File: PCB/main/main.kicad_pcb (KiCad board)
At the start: 2 copper layers, 97 x 73 mm, 64 parts, among them IC1 LM358DT, IC2 LM358DT, IC3 AT24C256C-SSHL-T, IC4 FT230XS-R, IC5 MCP73831T-2ACI_OT, IC6 MCP1700T-3302E_TT, J1 Conn_01x33_Female, J10 PZ254V-11-02P, J2 Conn_01x33_Female, J3 Conn_01x33_Female, J4 Conn_01x33_Female, J5 47346-0001, J6 PZ254V-11-02P, J7 PZ254V-11-02P, J8 MTP125-1103S1, J9 PZ254V-11-02P, Q1 IRF9540NPbF

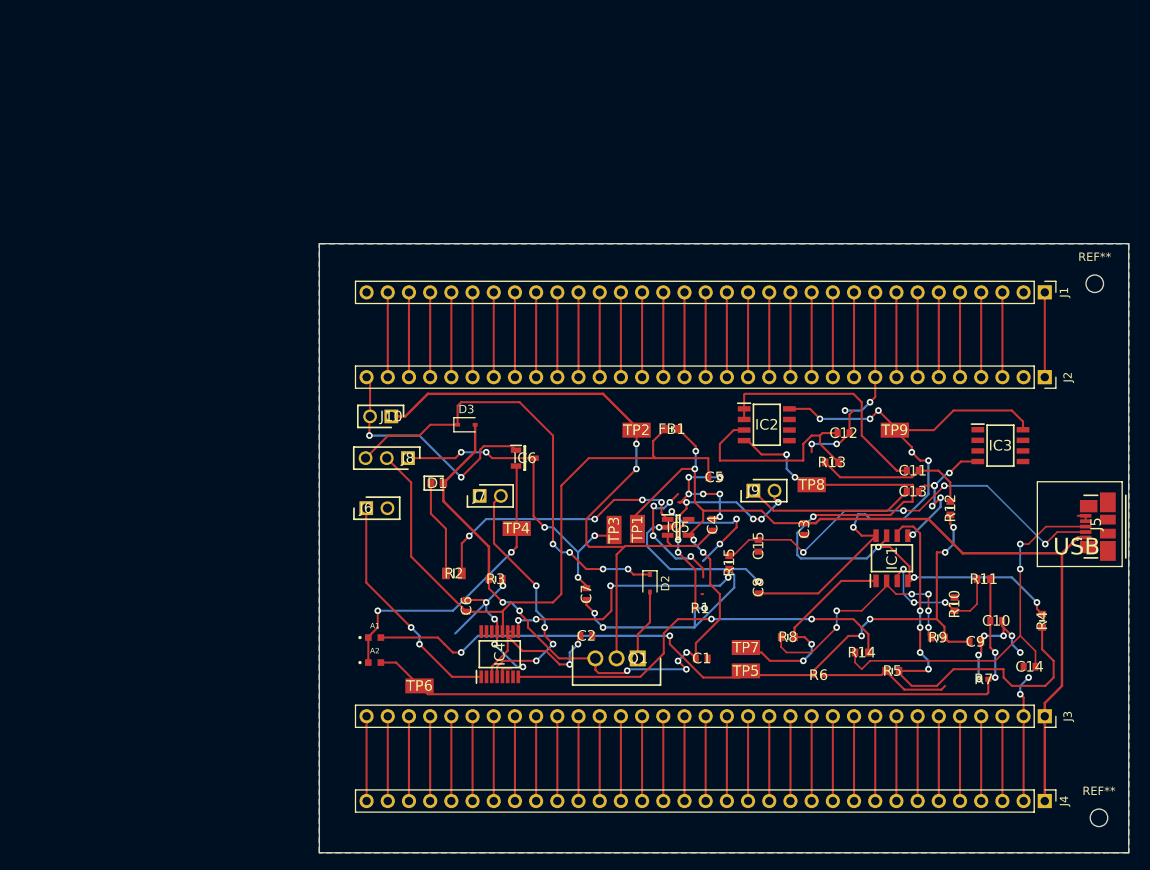
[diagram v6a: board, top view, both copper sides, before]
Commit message: changed power schematic
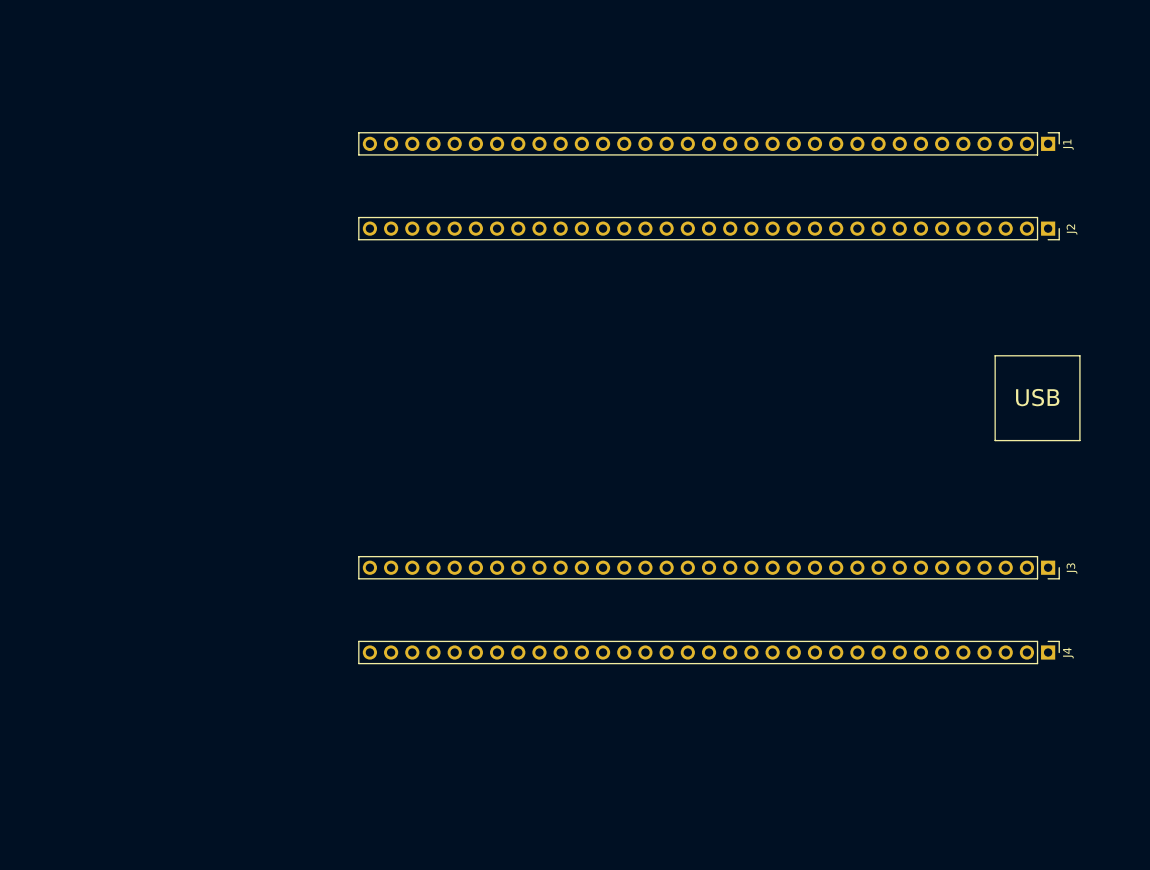
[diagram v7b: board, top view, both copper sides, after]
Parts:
- removed A1, A2: ALS-PT19-315C/L177/TR8, SamacSys_Parts:XDCR_ALS-PT19-315C_L177_TR8
- removed C1: 10nF, SamacSys_Parts:CAPC1608X90N
- removed C10, C9: CL10A105KB8NNNC, SamacSys_Parts:CAPC1608X90N
- removed C11, C12: CL10A335KP8NNNC, SamacSys_Parts:CAPC1608X90N
- removed C13, C2: CC0603KRX7R9BB104, SamacSys_Parts:CAPC1608X90N
- removed C14, C15: CL10C470JB8NNNC, SamacSys_Parts:CAPC1608X90N
- removed C3, C4, C6: CL10A475KA8NQNC, SamacSys_Parts_Microcontroller:CAPC1608X95N
- removed C5: 100nF, SamacSys_Parts:CAPC1608X90N
- removed C7, C8: 1uF, SamacSys_Parts:CAPC1608X90N
- removed D1: LED, SamacSys_Parts:LEDC1608X70N
- removed D2, D3: BAT60J, Diode_SMD:D_SOD-323
- removed FB1: Ferrite_Bead, SamacSys_Parts:BEADC1608X95N
- removed IC1, IC2: LM358DT, SamacSys_Parts:SOIC127P600X175-8N
- removed IC3: AT24C256C-SSHL-T, SamacSys_Parts:SOIC127P600X175-8N
- removed IC4: FT230XS-R, SamacSys_Parts_Power:SOP64P599X175-16N
- removed IC5: MCP73831T-2ACI_OT, SamacSys_Parts_Power:SOT95P270X145-5N
- removed IC6: MCP1700T-3302E_TT, SamacSys_Parts_Power:SOT95P237X112-3N
- removed J10, J6, J7, J9: PZ254V-11-02P, SamacSys_Parts_Power:HDRV2W64P0X254_1X2_508X250X873P
- removed J5: 47346-0001, SamacSys_Parts_Microcontroller:47346-0001
- removed J8: MTP125-1103S1, SamacSys_Parts_Power:HDRV3W64P0X254_1X3_762X250X885P
- removed Q1: IRF9540NPbF, SamacSys_Parts_Power:TO254P469X1042X1967-3P
- removed R1: 2k, SamacSys_Parts:RESC1005X35N
- removed R10, R11, R12, R13, R4, R5, R8, R9: RC0603FR-071KL, SamacSys_Parts:RESC1608X55N
- removed R14, R15: 0603WAF270JT5E, SamacSys_Parts:RESC1608X55N
- removed R2: RC0805FR-07470RL, SamacSys_Parts_Microcontroller:RESC2012X60N
- removed R3: 10k, SamacSys_Parts:RESC1608X55N
- removed R6, R7: AC0402FR-07536KL, SamacSys_Parts:RESC1005X37N
- removed REF** (x2): MountingHole_2.1mm, MountingHole:MountingHole_2.1mm
- removed TP1, TP2, TP3, TP4, TP5, TP6, TP7, TP8, TP9: 5017, SamacSys_Parts_Power:5017
- moved J4 17.8 mm to (180.3, 127.0)
- moved J1 17.8 mm to (180.3, 66.0)
- moved J2 17.8 mm to (180.3, 76.2)
- moved J3 17.8 mm to (180.3, 116.8)
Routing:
- net GND: track 244.5 -> 0.00 mm, vias 40 -> 0
- net +5V: track 180.9 -> 0.00 mm, vias 10 -> 0
- net +3v3: track 110.4 -> 0.00 mm, vias 8 -> 0
- net Vout1: track 94.9 -> 0.00 mm, vias 6 -> 0
- net Vout2: track 89.0 -> 0.00 mm, vias 2 -> 0
- net Net-(C4-Pad2): track 79.9 -> 0.00 mm, vias 2 -> 0
- net -3v3: track 78.4 -> 0.00 mm, vias 6 -> 0
- net VCC: track 75.1 -> 0.00 mm
- net Net-(D2-Pad1): track 54.4 -> 0.00 mm, vias 4 -> 0
- net IN2-: track 52.8 -> 0.00 mm, vias 4 -> 0
- net /Power/D-: track 50.9 -> 0.00 mm, vias 4 -> 0
- net Net-(IC4-Pad8): track 49.2 -> 0.00 mm, vias 2 -> 0
- net /Power/D+: track 47.2 -> 0.00 mm, vias 2 -> 0
- net Net-(C7-Pad1): track 39.8 -> 0.00 mm, vias 5 -> 0
- net Net-(IC5-Pad1): track 32.2 -> 0.00 mm, vias 4 -> 0
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- removed copper zone on B.Cu, net +3v3
- removed copper zone on F.Cu, net GND
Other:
- board outline removed

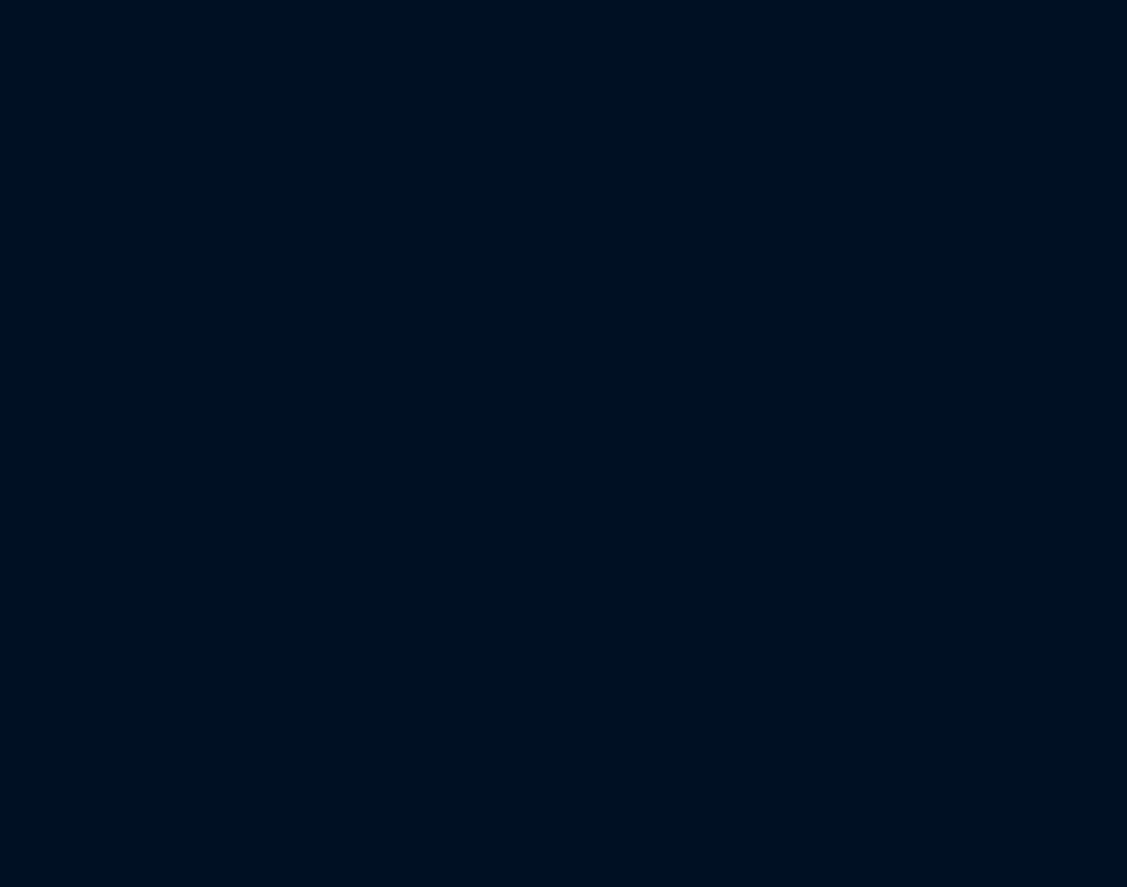
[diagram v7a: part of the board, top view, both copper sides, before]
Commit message: Week 5 submission, with improved version of the sensor
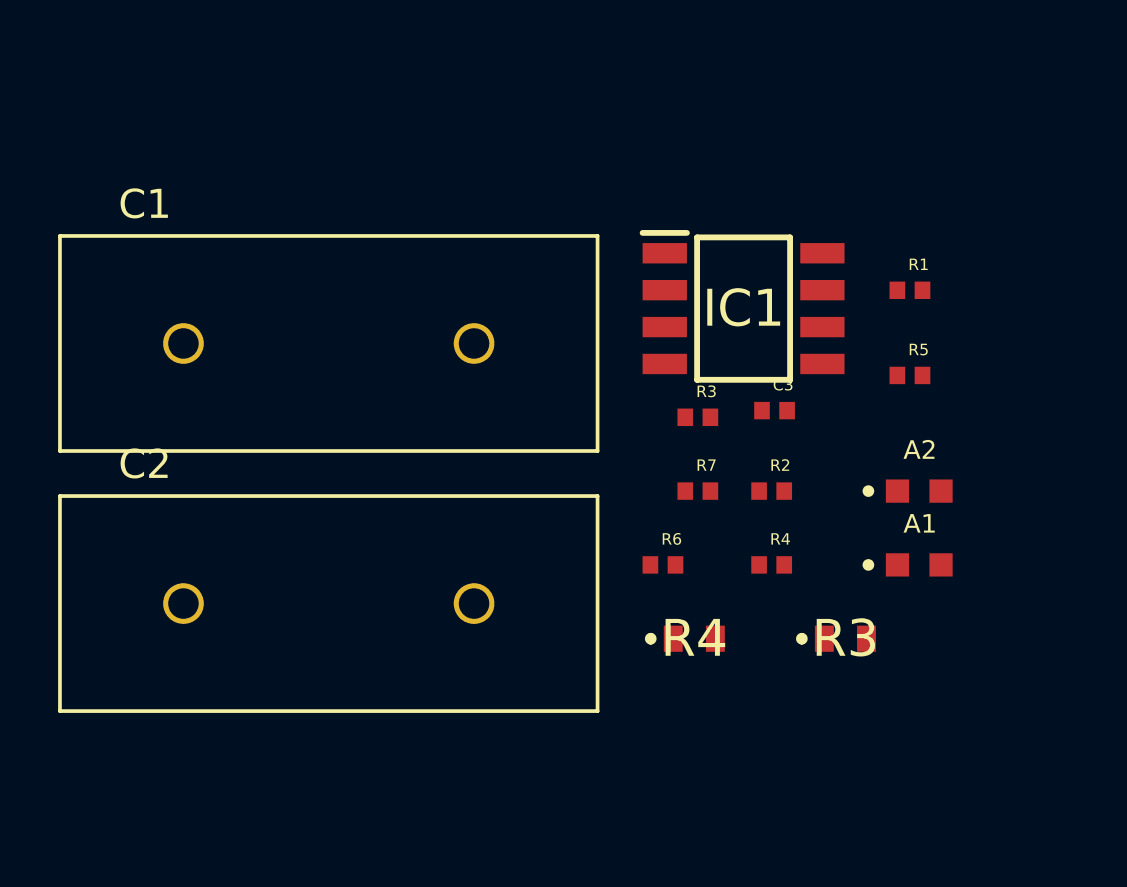
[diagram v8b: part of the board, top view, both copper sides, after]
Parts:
- added A1: ALS-PT19-315C/L177/TR8, footprints:XDCR_ALS-PT19-315C_L177_TR8, F.Cu at (86.4, 101.6)
- added A2: ALS-PT19-315C/L177/TR8, footprints:XDCR_ALS-PT19-315C_L177_TR8, F.Cu at (86.4, 99.1)
- added C1: ECQE2105KFB, footprints:CAPRR1000W80L1850T740H2000, F.Cu at (66.0, 94.0)
- added C2: ECQE2105KFB, footprints:CAPRR1000W80L1850T740H2000, F.Cu at (66.0, 102.9)
- added C3: GRM1555C1H5R1BA01D, footprints:CAPC1005X55N, F.Cu at (81.4, 96.3)
- added IC1: EL5171ISZ-T7, footprints:SOIC127P600X175-8N, F.Cu at (80.3, 92.8)
- added R1: AC0402FR-07536KL, footprints:RESC1005X37N, F.Cu at (86.0, 92.2)
- added R2: AC0402FR-07536KL, footprints:RESC1005X37N, F.Cu at (81.3, 99.1)
- added R3: ERJ3GEY0R00V, SamacSys_Parts:ERJ3EKF1000V, F.Cu at (83.8, 104.1)
- added R3: AC0402FR-07536KL, footprints:RESC1005X37N, F.Cu at (78.7, 96.5)
- added R4: ERJ3GEY0R00V, SamacSys_Parts:ERJ3EKF1000V, F.Cu at (78.6, 104.1)
- added R4: AC0402FR-07536KL, footprints:RESC1005X37N, F.Cu at (81.3, 101.6)
- added R5: AC0402FR-07536KL, footprints:RESC1005X37N, F.Cu at (86.0, 95.1)
- added R6: AC0402JR-0750RL, footprints:RESC1005X37N, F.Cu at (77.5, 101.6)
- added R7: AC0402JR-0750RL, footprints:RESC1005X37N, F.Cu at (78.7, 99.1)
